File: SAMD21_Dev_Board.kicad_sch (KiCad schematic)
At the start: 77 parts, among them J1 SWD, J10 JST_SH_SM06B-SRSS-TB_1x06-1MP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, J11 JST_SH_SM06B-SRSS-TB_1x06-1MP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, J12 JST_SH_SM06B-SRSS-TB_1x06-1MP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, J13 JST_SH_SM06B-SRSS-TB_1x06-1MP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, J14 JST_SH_SM06B-SRSS-TB_1x06-1MP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, J15 JST_SH_SM06B-SRSS-TB_1x06-1MP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, J16 JST_SH_SM06B-SRSS-TB_1x06-1MP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, J17 Status LED, J18 Screw_Terminal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

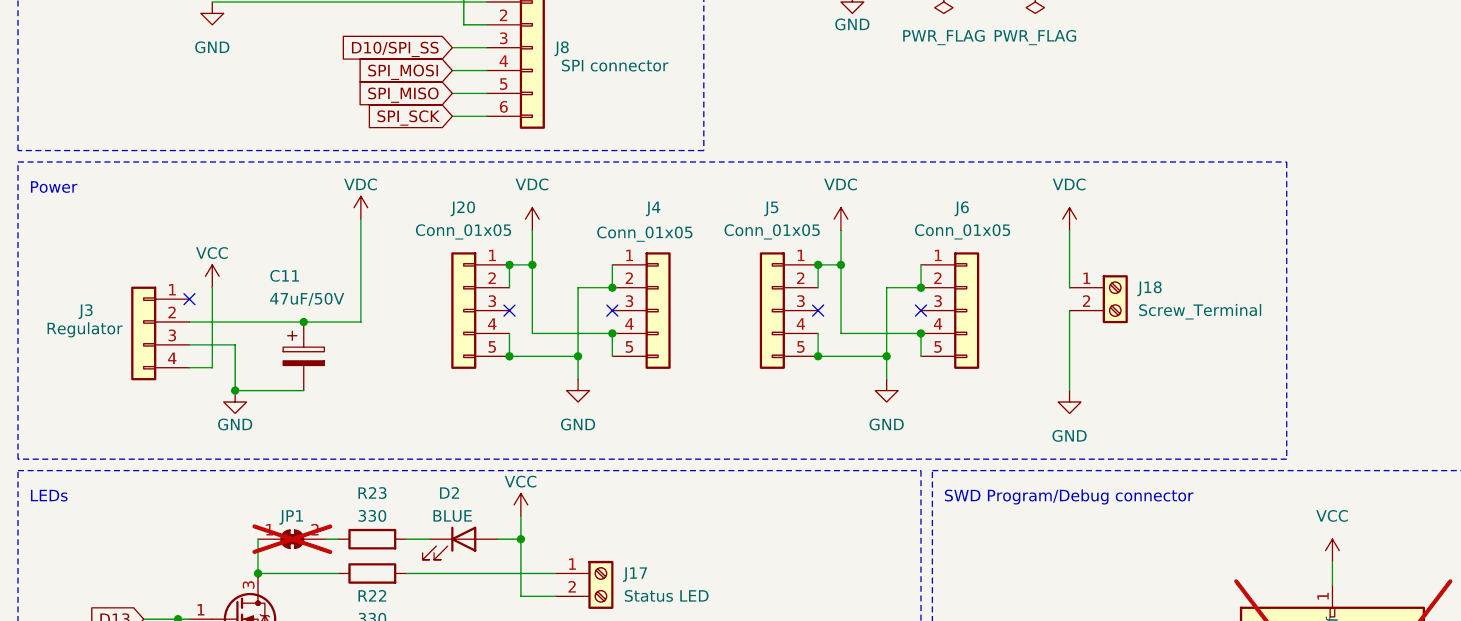
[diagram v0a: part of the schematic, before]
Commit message: SWD port moved closer to the edge to be able use the pogo pins clip
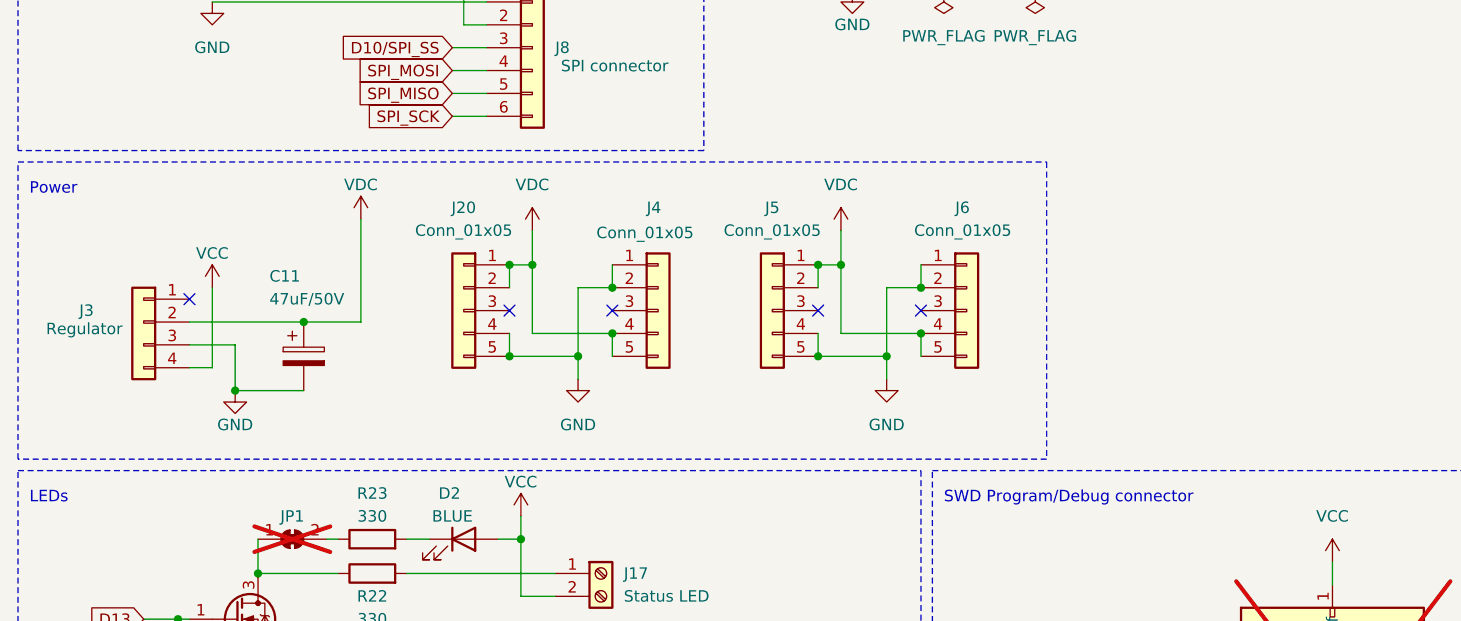
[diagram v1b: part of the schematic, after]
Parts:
- removed J18: Screw_Terminal, TerminalBlock_4Ucon:TerminalBlock_4Ucon_1x02_P3.50mm_Horizontal, symbol Connector:Screw_Terminal_01x02
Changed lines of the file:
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@@
 	(wire
 		(pts
-			(xy 132.08 196.85) (xy 132.08 203.2)
-		)
-		(stroke
-			(width 0)
-			(type default)
-		)
-	)
-	(wire
-		(pts
 			(xy 143.51 111.76) (xy 160.02 111.76)
 		)
@@
 	(wire
 		(pts
-			(xy 132.08 205.74) (xy 132.08 214.63)
-		)
-		(stroke
-			(width 0)
-			(type default)
-		)
-	)
-	(wire
-		(pts
 			(xy 104.14 200.66) (xy 106.68 200.66)
 		)
@@
 	(rectangle
 		(start 15.24 189.23)
-		(end 156.21 222.25)
+		(end 129.54 222.25)
 		(stroke
 			(width 0)
@@
 	)
 	(symbol
-		(lib_id "Connector:Screw_Terminal_01x02")
-		(at 137.16 203.2 0)
-		(unit 1)
-		(exclude_from_sim no)
-		(in_bom yes)
-		(on_board yes)
-		(dnp no)
-		(fields_autoplaced yes)
-		(property "Reference" "J18"
-			(at 139.7 203.2 0)
-			(effects
-				(font
-					(size 1.27 1.27)
-				)
-				(justify left)
-			)
-		)
-		(property "Value" "Screw_Terminal"
-			(at 139.7 205.74 0)
-			(effects
-				(font
-					(size 1.27 1.27)
-				)
-				(justify left)
-			)
-		)
-		(property "Footprint" "TerminalBlock_4Ucon:TerminalBlock_4Ucon_1x02_P3.50mm_Horizontal"
-			(at 137.16 203.2 0)
-			(effects
-				(font
-					(size 1.27 1.27)
-				)
-				(hide yes)
-			)
-		)
-		(property "Datasheet" "~"
-			(at 137.16 203.2 0)
-			(effects
-				(font
-					(size 1.27 1.27)
-				)
-				(hide yes)
-			)
-		)
-		(property "Description" ""
-			(at 137.16 203.2 0)
-			(effects
-				(font
-					(size 1.27 1.27)
-				)
-				(hide yes)
-			)
-		)
-		(property "MPN" "C695629"
-			(at 137.16 203.2 0)
-			(effects
-				(font
-					(size 1.27 1.27)
-				)
-				(hide yes)
-			)
-		)
-		(property "Feeder" ""
-			(at 137.16 203.2 0)
-			(effects
-				(font
-					(size 1.27 1.27)
-				)
-				(hide yes)
-			)
-		)
-		(pin "1"
-		)
-		(pin "2"
-		)
-		(instances
-			(project "SAMD21_Dev_Board"
-				(path "/1a1c72da-99f5-4976-b608-38ee505f2b67"
-					(reference "J18")
-					(unit 1)
-				)
-			)
-		)
-	)
-	(symbol
 		(lib_id "Device:C")
 		(at 271.78 238.76 0)
@@
 	)
 	(symbol
-		(lib_id "power:VDC")
-		(at 132.08 196.85 0)
-		(unit 1)
-		(exclude_from_sim no)
-		(in_bom yes)
-		(on_board yes)
-		(dnp no)
-		(fields_autoplaced yes)
-		(property "Reference" "#PWR052"
-			(at 132.08 199.39 0)
-			(effects
-				(font
-					(size 1.27 1.27)
-				)
-				(hide yes)
-			)
-		)
-		(property "Value" "VDC"
-			(at 132.08 191.77 0)
-			(effects
-				(font
-					(size 1.27 1.27)
-				)
-			)
-		)
-		(property "Footprint" ""
-			(at 132.08 196.85 0)
-			(effects
-				(font
-					(size 1.27 1.27)
-				)
-				(hide yes)
-			)
-		)
-		(property "Datasheet" ""
-			(at 132.08 196.85 0)
-			(effects
-				(font
-					(size 1.27 1.27)
-				)
-				(hide yes)
-			)
-		)
-		(property "Description" "Power symbol creates a global label with name \"VDC\""
-			(at 132.08 196.85 0)
-			(effects
-				(font
-					(size 1.27 1.27)
-				)
-				(hide yes)
-			)
-		)
-		(pin "1"
-		)
-		(instances
-			(project "SAMD21_Dev_Board"
-				(path "/1a1c72da-99f5-4976-b608-38ee505f2b67"
-					(reference "#PWR052")
-					(unit 1)
-				)
-			)
-		)
-	)
-	(symbol
 		(lib_id "power:GND")
 		(at 39.37 214.63 0)
@@
 					(unit 1)
 				)
-			)
-		)
-	)
-	(symbol
-		(lib_id "power:GND")
-		(at 132.08 214.63 0)
-		(unit 1)
-		(exclude_from_sim no)
-		(in_bom yes)
-		(on_board yes)
-		(dnp no)
-		(fields_autoplaced yes)
-		(property "Reference" "#PWR051"
-			(at 132.08 220.98 0)
-			(effects
-				(font
-					(size 1.27 1.27)
-				)
-				(hide yes)
-			)
-		)
-		(property "Value" "GND"
-			(at 132.08 219.71 0)
-			(effects
-				(font
-					(size 1.27 1.27)
-				)
-			)
-		)
-		(property "Footprint" ""
-			(at 132.08 214.63 0)
-			(effects
-				(font
-					(size 1.27 1.27)
-				)
-				(hide yes)
-			)
-		)
-		(property "Datasheet" ""
-			(at 132.08 214.63 0)
-			(effects
-				(font
-					(size 1.27 1.27)
-				)
-				(hide yes)
-			)
-		)
-		(property "Description" "Power symbol creates a global label with name \"GND\" , ground"
-			(at 132.08 214.63 0)
-			(effects
-				(font
-					(size 1.27 1.27)
-				)
-				(hide yes)
-			)
-		)
-		(pin "1"
-		)
-		(instances
-			(project "SAMD21_Dev_Board"
-				(path "/1a1c72da-99f5-4976-b608-38ee505f2b67"
-					(reference "#PWR051")
-					(unit 1)
-				)

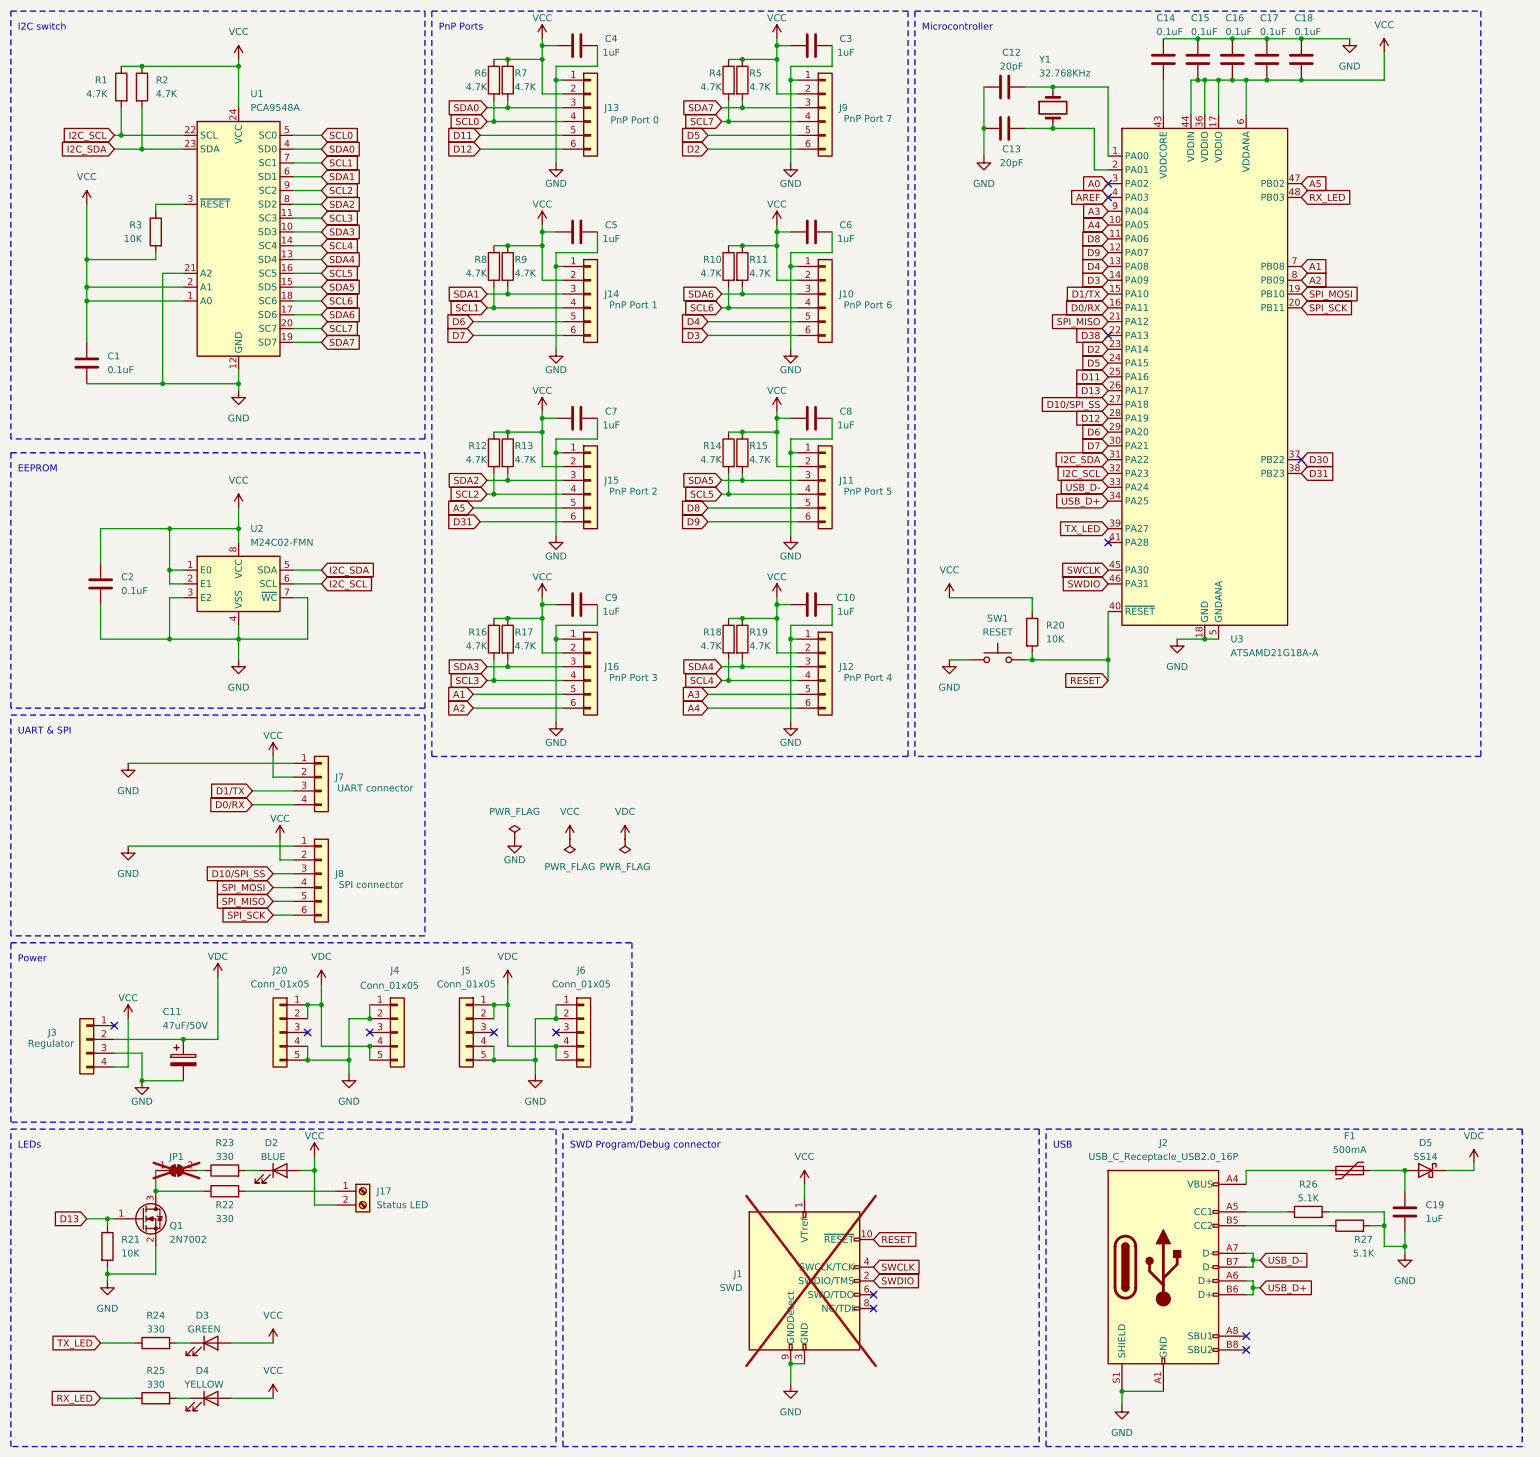
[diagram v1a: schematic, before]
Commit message: Fiducials change to 1mm footprint Using D4 line for status LED (can do PWM) instead of D13 Bootloader updated accordingly
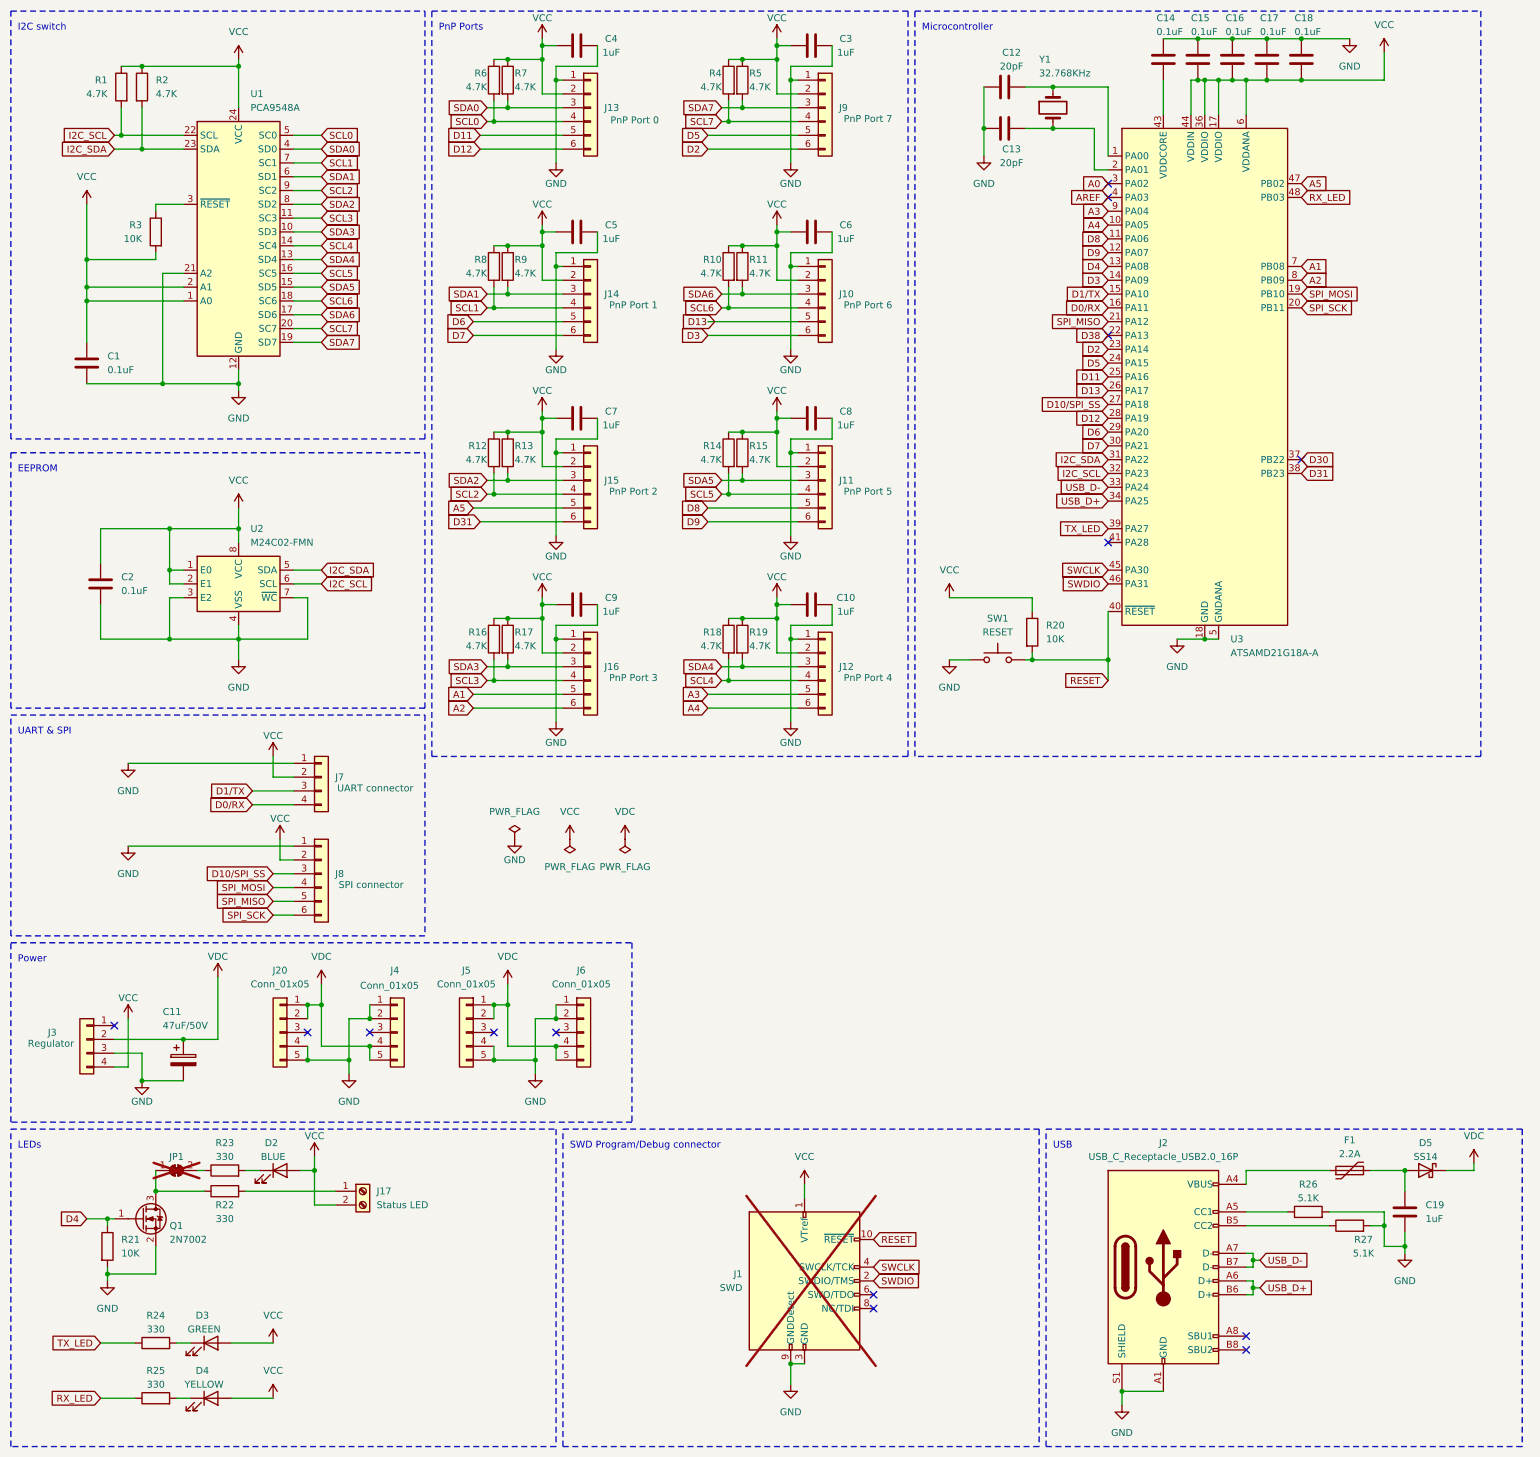
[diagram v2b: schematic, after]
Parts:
- F1: value 500mA -> 2.2A; MPN C883126 -> C89654
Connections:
- net D13: now also J10.5 (Pin_5); no longer Q1.1 (G), R21.1
- net D4: now also Q1.1 (G), R21.1; no longer J10.5 (Pin_5)
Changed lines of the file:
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@@
 		)
 	)
-	(global_label "D4"
+	(global_label "D13"
 		(shape input)
-		(at 143.51 74.93 180)
+		(at 144.78 74.93 180)
 		(fields_autoplaced yes)
 		(effects
@@
 		)
 		(property "Intersheetrefs" "${INTERSHEET_REFS}"
-			(at 138.0453 74.93 0)
+			(at 138.1058 74.93 0)
 			(effects
 				(font
@@
 		)
 	)
-	(global_label "D13"
+	(global_label "D4"
 		(shape input)
 		(at 29.21 240.03 180)
@@
 		)
 		(property "Intersheetrefs" "${INTERSHEET_REFS}"
-			(at 22.5358 240.03 0)
+			(at 23.7453 240.03 0)
 			(effects
 				(font
@@
 		(on_board yes)
 		(dnp no)
-		(fields_autoplaced yes)
 		(property "Reference" "F1"
-			(at 261.62 224.79 90)
+			(at 261.62 225.552 90)
 			(effects
 				(font
@@
 			)
 		)
-		(property "Value" "500mA"
-			(at 261.62 227.33 90)
+		(property "Value" "2.2A"
+			(at 261.62 228.092 90)
 			(effects
 				(font
@@
 			)
 		)
-		(property "MPN" "C883126"
+		(property "MPN" "C89654"
 			(at 261.62 231.14 0)
 			(effects
